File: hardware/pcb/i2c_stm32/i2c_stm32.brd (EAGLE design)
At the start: 24.1 x 78.7 mm, 54 parts, among them U1 STM32F103C8T6, U2 MPU-6050, U3 BMP280, U4 NRF24L01, U5 RT9193-33GB, Y1 8MHz, Y3 16MHz, Y4 32.768kHz

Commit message: schematic updates
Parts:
- removed C14: 10nF, Resistor_Capacitor:CAP_0603
- removed C15: 1nF, Resistor_Capacitor:CAP_0603
- removed R4: RC0603JR-070RL, Resistor_Capacitor:RES_0603
- removed U$1: 2.7 nH, Nordic_nRF:RESC0603_M
- removed U$2: 8.2 nH, Nordic_nRF:RESC0603_M
- removed U$3: 3.9 nH, Nordic_nRF:RESC0603_M
- added L1: 2.7 nH, Nordic_nRF:RESC0603_M
- added L2: 8.2 nH, Nordic_nRF:RESC0603_M
- added L3: 3.9 nH, Nordic_nRF:RESC0603_M
- added R6: 220, Resistor_Capacitor:RES_0603
- C10: value 100 nF -> 1pF
- C16, C17: value 22pF -> 15pF
- C30, C31: value 22pF -> 10pF
- C4: value 0.01 uF -> 0.01uF
- C7, C8: value 22pF -> 18pF
- C9: value 100 nF -> 1.5pF
- R1: value RC0603JR-070RL -> 220
- moved J3 87.6 mm to (-63.5, 31.8), turned to 0 degrees
- moved J5 83.1 mm to (-33.0, 5.08), turned to 0 degrees
- moved U2 78.4 mm to (-54.6, 5.08)
- moved U4 76.5 mm to (-45.7, 6.35)
- moved U3 75.6 mm to (-49.5, 19.1)
- moved J4 73.8 mm to (-63.5, 35.6), turned to 0 degrees
- moved Y1 66.2 mm to (-54.6, 17.8)
- moved U5 64.9 mm to (-22.9, 25.4)
- moved U$4 57.0 mm to (-29.2, 26.7), turned to 0 degrees
- moved C25 52.8 mm to (-15.2, 48.3)
- moved Y3 49.5 mm to (-16.5, 26.7)
- moved C26 48.5 mm to (-19.1, 48.3)
- moved J2 47.3 mm to (-22.9, 39.4)
- moved Y4 46.4 mm to (-35.6, 25.4)
- moved C27 44.5 mm to (-22.9, 48.3)
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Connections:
- net BMP_SCK renamed BMP_SCL
- net SCL renamed IMU_SCL
- removed net N$10: U$1.1, U$2.1, U4.12
- removed net N$11: U$2.2, U$3.1, U4.13
- removed net SDA: U2.24, U3.3
- new net ANT1: L1.1, L2.1, U4.12
- new net ANT2: L2.2, L3.1, U4.13
- new net BMP_SDA: U3.3
- new net IMU_SDA: U2.24
- net GND: no longer C14.2, C15.2
- net N$13: now also L3.2; no longer U$3.2
- net N$4: now also R6.2; no longer R1.2
- net N$6: now also R1.2; no longer R4.2
- net PC13: now also R1.1; no longer R4.1
- net VDD: now also R6.1; no longer C14.1, C15.1, R1.1
- net VDD_PA: now also L1.2; no longer U$1.2
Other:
- board size 24.1 x 78.7 mm -> 160 x 100 mm

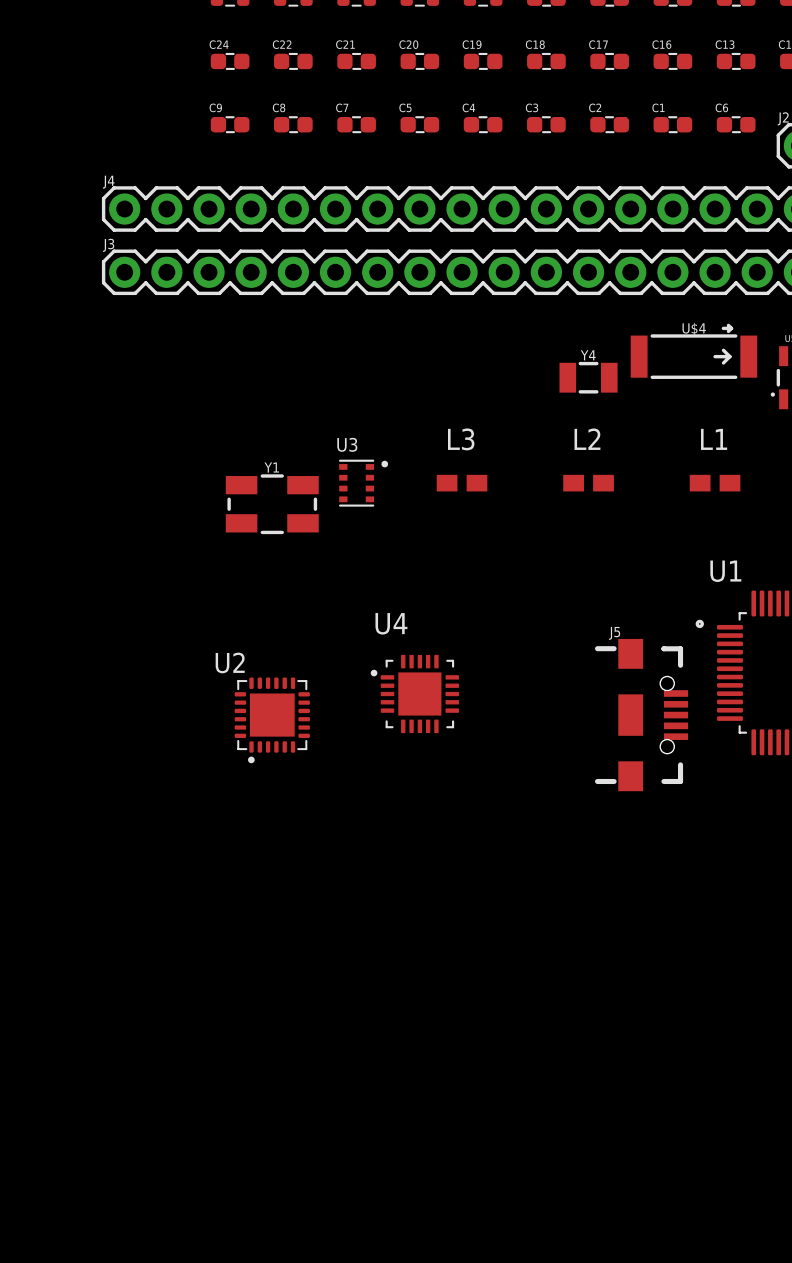
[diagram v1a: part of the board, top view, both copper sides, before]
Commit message: Replaced BMP280 w/ BMP388 cause of stock availability and another tweaks to schematic
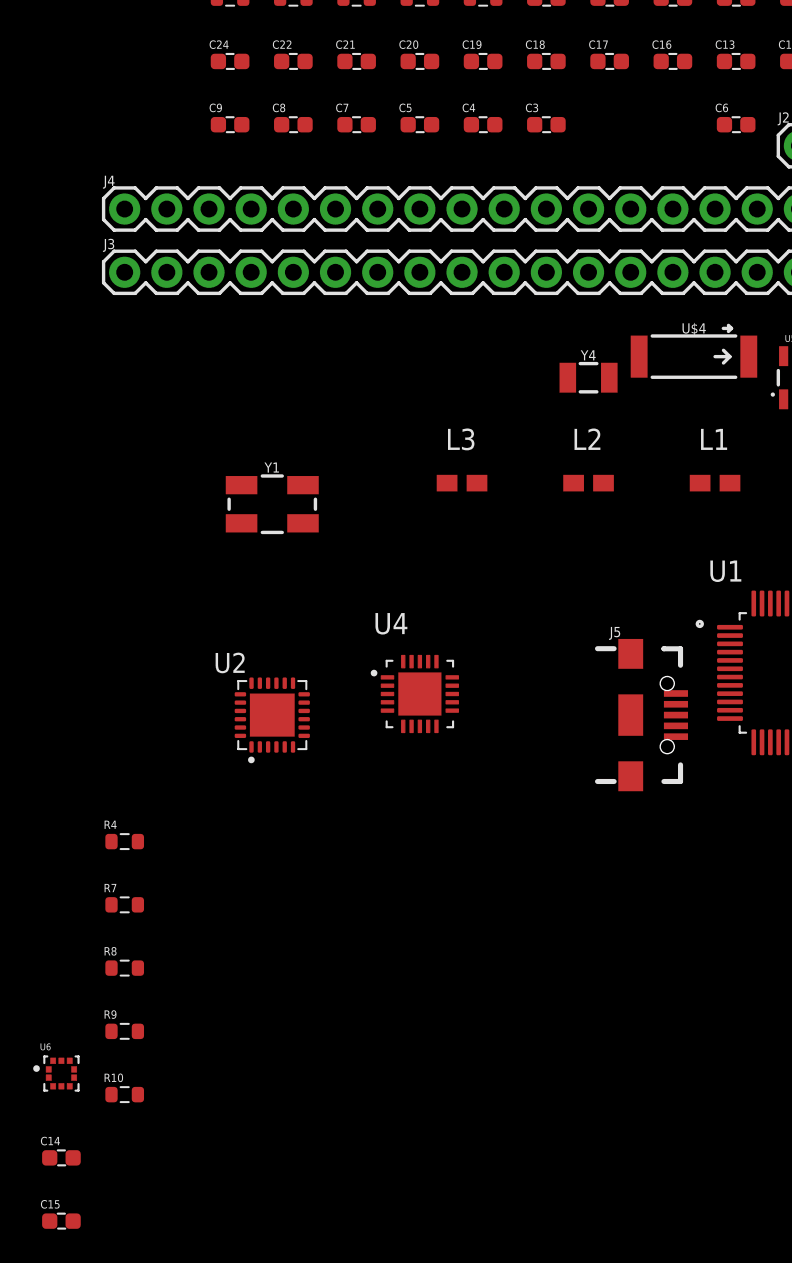
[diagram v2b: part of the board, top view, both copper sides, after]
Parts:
- removed C1, C2: 100 nF, Resistor_Capacitor:CAP_0603
- removed U3: BMP280, BMP280:XDCR_BMP280
- added C14, C15: 100 nF, Resistor_Capacitor:CAP_0603
- added R10, R7, R8, R9: 4.7k, Resistor_Capacitor:RES_0603
- added R4: 1M, Resistor_Capacitor:RES_0603
- added U6: BMP388, BMP388:PQFN50P200X200X80-10N
- C3: value 0.1 uF -> 100nF
- C6: value 2200 pF -> 2.2nF
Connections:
- removed net BMP_SCL: U3.4
- removed net BMP_SDA: U3.3
- removed net CE: U4.1
- removed net CSN: U4.2
- removed net IMU_INT: U2.12
- removed net IMU_SCL: U2.23
- removed net IMU_SDA: U2.24
- removed net IRQ: U4.6
- removed net MISO: U4.5
- removed net MOSI: U4.4
- removed net N$15: U3.5
- removed net SCK: U4.3
- net GND: now also C14.2, C15.1, U6.3, U6.5, U6.8, U6.9; no longer C1.1, C2.2, U3.1, U3.7
- net N$7: now also R4.2
- net N$8: now also R4.1
- net PA1: now also U2.12
- net PA4: now also U4.1
- net PA5: now also U4.3
- net PA6: now also U4.5
- net PA7: now also U4.4
- net PB0: now also U4.2
- net PB1: now also U4.6
- net PB10: now also R9.1, U2.23
- net PB11: now also R10.1, U2.24
- net PB6: now also R7.1, U6.2
- net PB7: now also R8.1, U6.4
- net PB9: now also U6.7
- net VDD: now also C14.1, C15.2, R10.2, R7.2, R8.2, R9.2, U6.1, U6.10, U6.6; no longer C1.2, C2.1, U3.2, U3.6, U3.8

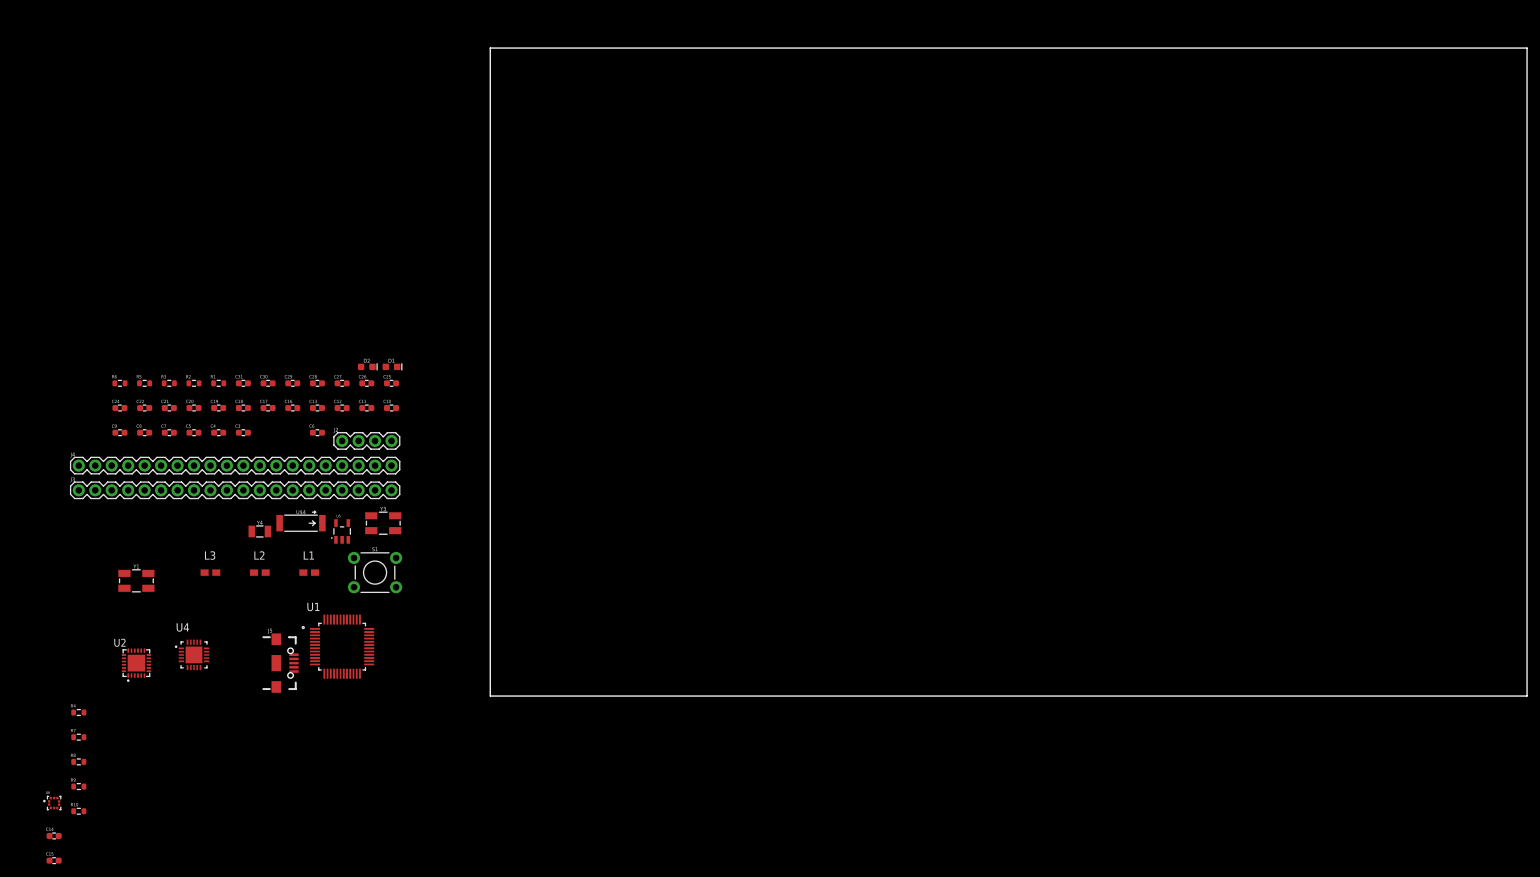
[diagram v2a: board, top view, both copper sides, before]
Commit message: Schematic finished, BOM verified
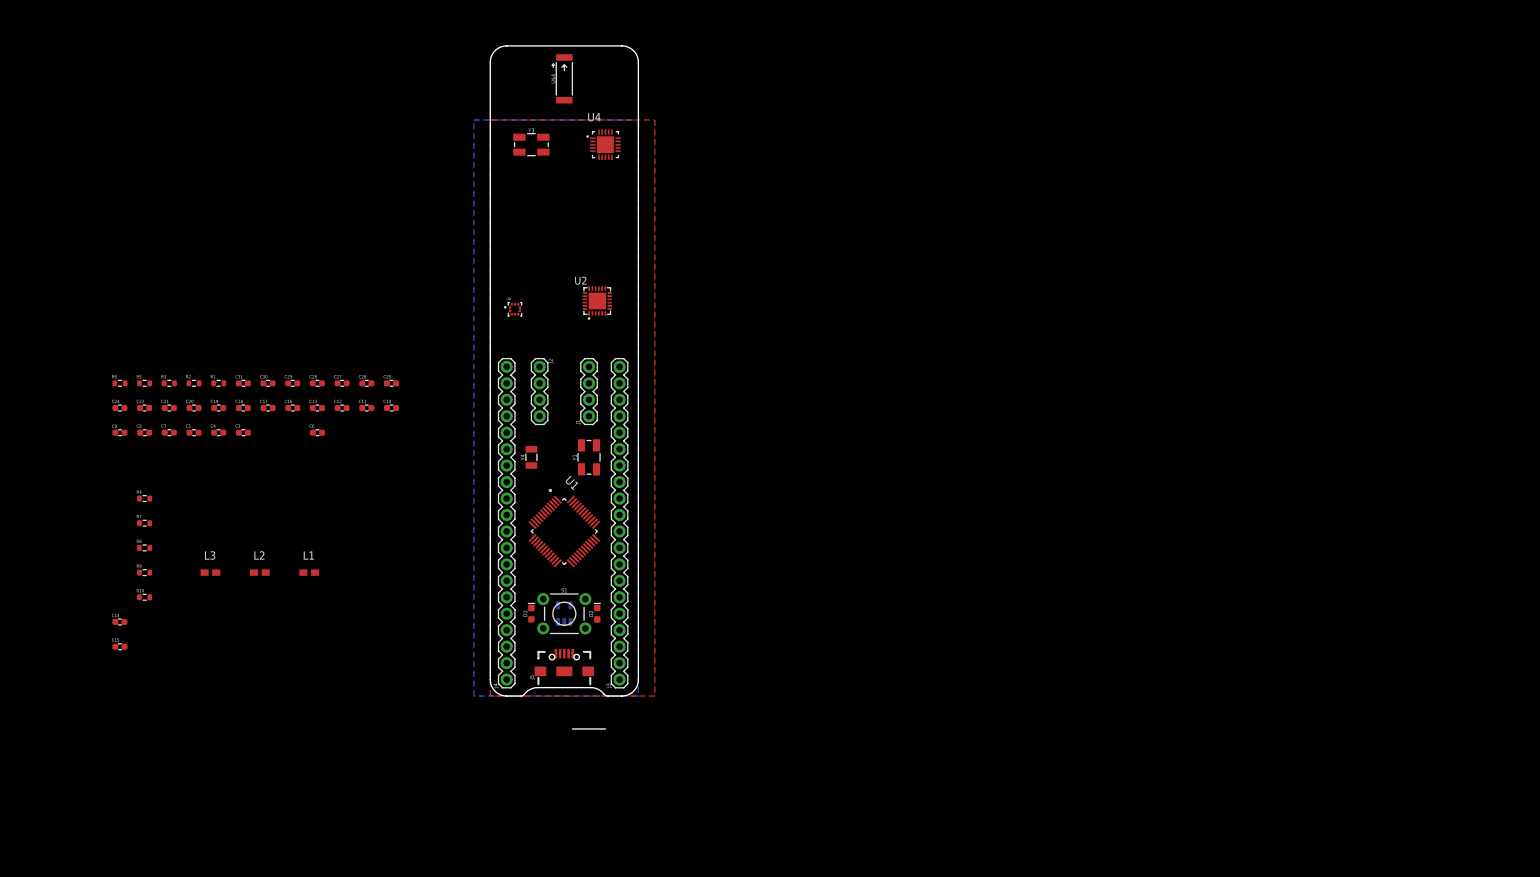
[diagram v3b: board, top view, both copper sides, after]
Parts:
- added J1: (no value), SparkFun-Connectors:1X04
- moved U6 104.2 mm to (3.81, 59.7)
- moved U4 101.2 mm to (17.8, 85.1)
- moved U2 90.4 mm to (16.5, 61.0)
- moved J3 88.4 mm to (20.0, 2.54), turned to 90 degrees
- moved U$4 79.7 mm to (11.4, 95.2), turned to 90 degrees
- moved J4 73.8 mm to (2.54, 2.54), turned to 90 degrees
- moved Y1 72.4 mm to (15.2, 36.8), turned to 90 degrees
- moved Y3 62.7 mm to (6.35, 85.1)
- moved D2 52.1 mm to (16.5, 12.7), turned to 90 degrees
- moved J5 44.5 mm to (11.4, 3.81), turned to 90 degrees
- moved D1 43.8 mm to (6.35, 12.7), turned to 90 degrees
- moved Y4 43.4 mm to (6.35, 36.8), turned to 90 degrees
- moved U1 38.6 mm to (11.4, 25.4), turned to 315 degrees
- moved U5 36.6 mm to (11.4, 12.7), flipped to the bottom
- moved C14 34.5 mm to (-57.1, 11.4)
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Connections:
- removed net N$1: C4.1, U2.8
- net GND: now also J1.1
- net PA10: now also J1.2
- net PA9: now also J1.3
- net VDD: now also C4.1, J1.4, U2.8
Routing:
- added copper zone on layer 1, net GND
- added copper zone on layer 16, net VDD
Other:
- board size 160 x 100 mm -> 22.9 x 105.4 mm

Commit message: finalized circuit boards and ordered w/ gerber files
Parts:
- moved C15 93.6 mm to (16.8, 65.0), turned to 90 degrees
- moved R4 91.4 mm to (18.8, 86.6)
- moved R10 90.7 mm to (19.3, 69.6), turned to 270 degrees
- moved C14 89.7 mm to (14.7, 65.0), turned to 270 degrees
- moved L3 86.9 mm to (5.59, 90.9), turned to 180 degrees
- moved L2 85.9 mm to (11.4, 90.9), turned to 180 degrees
- moved R9 85.4 mm to (16.0, 68.8), turned to 180 degrees
- moved L1 84.9 mm to (17.3, 90.9)
- moved C8 83.5 mm to (20.8, 79.0), turned to 270 degrees
- moved C24 78.8 mm to (14.7, 12.2), turned to 90 degrees
- moved C7 76.6 mm to (16.8, 79.0), turned to 270 degrees
- moved C9 76.2 mm to (1.78, 88.9), turned to 270 degrees
- moved R8 69.8 mm to (2.29, 65.0), turned to 90 degrees
- moved R7 69.7 mm to (4.83, 65.0), turned to 90 degrees
- moved R3 69.2 mm to (12.4, 17.5), turned to 180 degrees
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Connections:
- removed net N$14: C25.1, C26.1, U5.2
- removed net PA13: J4.19
- removed net PA14: J4.18
- removed net PB2: U1.20
- removed net VBAT: J3.1, U1.1
- net GND: now also C25.1, C26.1, U1.20, U5.2
- net PA1: no longer U2.12
- net PA12: no longer J4.20
- net PB12: now also J4.20
- net PB13: now also J4.19
- net PB14: now also J4.18
- net PB9: no longer U6.7
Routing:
- net VDD: track 0.00 -> 110.6 mm, vias 0 -> 13
- net PA4: track 0.00 -> 97.2 mm, vias 0 -> 1
- net PB7: track 0.00 -> 88.5 mm, vias 0 -> 2
- net PA5: track 0.00 -> 88.4 mm, vias 0 -> 3
- net PB1: track 0.00 -> 86.9 mm, vias 0 -> 2
- net PA6: track 0.00 -> 84.2 mm, vias 0 -> 3
- net PC13: track 0.00 -> 81.0 mm, vias 0 -> 3
- net PB0: track 0.00 -> 78.0 mm
- net PB6: track 0.00 -> 78.0 mm
- net PB11: track 0.00 -> 77.4 mm, vias 0 -> 2
- net PA7: track 0.00 -> 75.8 mm
- net PB10: track 0.00 -> 74.6 mm, vias 0 -> 2
- net RESET: track 0.00 -> 61.3 mm, vias 0 -> 4
- net PA10: track 0.00 -> 53.4 mm, vias 0 -> 2
- net PA9: track 0.00 -> 52.4 mm, vias 0 -> 2
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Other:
- board size 22.9 x 105.4 mm -> 23.3 x 105.4 mm
- board text added: "5V"
- board text added: "C:/Users/cbaro/OneDrive/Pictures/picodrone.bmp"
- board text added: "GND"
- board text added: "PA0"
- board text added: "PA1"
- board text added: "PA10"
- board text added: "PA11"
- board text added: "PA12"
- board text added: "PA15"
- board text added: "PA2"
- board text added: "PA3"
- board text added: "PA4"
- board text added: "PA5"
- board text added: "PA6"
- board text added: "PA7"
- board text added: "PA8"
- board text added: "PA9"
- board text added: "PB0"
- board text added: "PB1"
- board text added: "PB10"
- board text added: "PB11"
- board text added: "PB12"
- board text added: "PB13"
- board text added: "PB14"
- board text added: "PB15"
- board text added: "PB3"
- board text added: "PB4"
- board text added: "PB5"
- board text added: "PB6"
- board text added: "PB7"
- board text added: "PB8"
- board text added: "PB9"
- board text added: "PC13"
- board text added: "PC14"
- board text added: "PC15"
- board text added: "RST"
- board text added: "RX"
- board text added: "SWCLK"
- board text added: "SWDIO"
- board text added: "TX"
- board text added: "VDD"
